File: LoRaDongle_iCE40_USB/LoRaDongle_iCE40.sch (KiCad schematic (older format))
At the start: 19 parts, among them J1 USB_A, J2 Conn_01x08

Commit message: PCB Layout V01
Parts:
- removed TP5: iCE_SCK, TestPoint:TestPoint_Pad_D2.5mm, symbol Connector:TestPoint_Small
- 5V0: renamed from TP4; footprint TestPoint:TestPoint_Pad_D2.5mm -> TestPoint:TestPoint_Pad_D1.0mm
- BUSY1: renamed from TP13; footprint TestPoint:TestPoint_Pad_D2.5mm -> TestPoint:TestPoint_Pad_D1.0mm
- C1: footprint Capacitor_SMD:C_0402_1005Metric -> Capacitor_SMD:C_0402_1005Metric_Pad0.74x0.62mm_HandSolder
- CDNE1: renamed from TP7; footprint TestPoint:TestPoint_Pad_D2.5mm -> TestPoint:TestPoint_Pad_D1.0mm
- CRST1: renamed from TP8; footprint TestPoint:TestPoint_Pad_D2.5mm -> TestPoint:TestPoint_Pad_D1.0mm
- DIO1: renamed from TP10; footprint TestPoint:TestPoint_Pad_D2.5mm -> TestPoint:TestPoint_Pad_D1.0mm
- L_SS1: renamed from TP12; value LoRa!_SS -> LoRa_!SS; footprint TestPoint:TestPoint_Pad_D2.5mm -> TestPoint:TestPoint_Pad_D1.0mm
- MISO1: renamed from TP15; footprint TestPoint:TestPoint_Pad_D2.5mm -> TestPoint:TestPoint_Pad_D1.0mm
- MOSI1: renamed from TP11; footprint TestPoint:TestPoint_Pad_D2.5mm -> TestPoint:TestPoint_Pad_D1.0mm
- R1, R2: footprint Resistor_SMD:R_0402_1005Metric -> Resistor_SMD:R_0402_1005Metric_Pad0.72x0.64mm_HandSolder
- RESET1: renamed from TP9; value LoRa_~RESET -> LoRA_~RESET; footprint TestPoint:TestPoint_Pad_D2.5mm -> TestPoint:TestPoint_Pad_D1.0mm
- SCK1: renamed from TP14; footprint TestPoint:TestPoint_Pad_D2.5mm -> TestPoint:TestPoint_Pad_D1.0mm
- SS_B1: renamed from TP6; footprint TestPoint:TestPoint_Pad_D2.5mm -> TestPoint:TestPoint_Pad_D1.0mm
- renumbered JP1 to J4
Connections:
- net ICE_CDONE: now also J2.2 (Pin_2); no longer J2.5 (Pin_5)
- net ICE_CRESET: now also J2.1 (Pin_1); no longer J2.6 (Pin_6)
- net SPI_MISO: now also J2.4 (Pin_4); no longer J2.3 (Pin_3)
- net SPI_MOSI: now also J2.5 (Pin_5); no longer J2.2 (Pin_2)
- net SPI_SCK: now also J2.6 (Pin_6); no longer J2.1 (Pin_1)
- net SPI_SS: now also J2.3 (Pin_3); no longer J2.4 (Pin_4)
- net V_USB: now also J4.1; no longer J4.3
- net V_conn: now also J4.3; no longer J4.1
- net D-: now reaches J1.2 (D-), R2.2
- net D+: now reaches J1.3 (D+), R1.2
- net USB_Interface/DM renamed USB_Interface/USB_D-
- net USB_Interface/DP renamed USB_Interface/UBS_D+
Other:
- moved on the sheet: CDNE1, CRST1, SS_B1
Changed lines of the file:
@@
 $EndComp
 $Comp
-L Device:Jumper_NC_Dual JP1
+L Device:Jumper_NC_Dual J4
 U 1 1 616C0AFF
 P 3950 1800
-F 0 "JP1" H 3950 1947 50  0000 C CNN
+F 0 "J4" H 3950 1947 50  0000 C CNN
 F 1 "Jumper" H 3950 2038 50  0000 C CNN
 F 2 "Connector_PinHeader_2.54mm:PinHeader_1x03_P2.54mm_Vertical" H 3950 1800 50  0001 C CNN
@@
 	-1   0    0    1
 $EndComp
-Text Label 4400 1800 0    50   ~ 0
-V_conn
-Text Label 3550 1800 2    50   ~ 0
+Text Label 4350 1800 0    50   ~ 0
 V_USB
 Wire Wire Line
-	3550 1800 3700 1800
-Wire Wire Line
-	4200 1800 4400 1800
+	4350 1800 4200 1800
 $Comp
 L power:+5V #PWR03
@@
 F 0 "C1" H 2150 1750 50  0000 C CNN
 F 1 "0.1uF" H 2100 2000 50  0000 C CNN
-F 2 "Capacitor_SMD:C_0402_1005Metric" H 2288 1700 50  0001 C CNN
+F 2 "Capacitor_SMD:C_0402_1005Metric_Pad0.74x0.62mm_HandSolder" H 2288 1700 50  0001 C CNN
 F 3 "~" H 2250 1850 50  0001 C CNN
 F 4 "GCM155R71C104KA55J" V 2250 1850 50  0001 C CNN "Part Number"
@@
 F 0 "R2" V 2100 3950 50  0000 C CNN
 F 1 "10R" V 2000 3950 50  0000 C CNN
-F 2 "Resistor_SMD:R_0402_1005Metric" V 1930 3950 50  0001 C CNN
+F 2 "Resistor_SMD:R_0402_1005Metric_Pad0.72x0.64mm_HandSolder" V 1930 3950 50  0001 C CNN
 F 3 "~" H 2000 3950 50  0001 C CNN
 	1    2000 3950
@@
 F 0 "R1" V 1900 3850 50  0000 C CNN
 F 1 "10R" V 2000 3850 50  0000 C CNN
-F 2 "Resistor_SMD:R_0402_1005Metric" V 1930 3850 50  0001 C CNN
+F 2 "Resistor_SMD:R_0402_1005Metric_Pad0.72x0.64mm_HandSolder" V 1930 3850 50  0001 C CNN
 F 3 "~" H 2000 3850 50  0001 C CNN
 	1    2000 3850
@@
 F0 "USB_Interface" 50
 F1 "USB_Interface.sch" 50
-F2 "DP" I L 2300 3850 50
-F3 "DM" I L 2300 3950 50
-F4 "SPI_SCK" O R 3650 3650 50
-F5 "SPI_MOSI" O R 3650 3750 50
-F6 "SPI_MISO" O R 3650 3850 50
-F7 "SPI_SS" O R 3650 3950 50
-F8 "iCE_CDONE" O R 3650 4100 50
-F9 "iCE_CRESET" O R 3650 4200 50
+F2 "SPI_SCK" O R 3650 3650 50
+F3 "SPI_MOSI" O R 3650 3750 50
+F4 "SPI_MISO" O R 3650 3850 50
+F5 "SPI_SS" O R 3650 3950 50
+F6 "iCE_CDONE" O R 3650 4100 50
+F7 "iCE_CRESET" O R 3650 4200 50
+F8 "USB_D-" I L 2300 3950 50
+F9 "UBS_D+" I L 2300 3850 50
 $EndSheet
 Text Notes 5900 1250 0    50   ~ 0
@@
 	6350 2150 6500 2150
 Wire Wire Line
-	6350 2050 6450 2050
-Wire Wire Line
-	6350 1950 6450 1950
-Wire Wire Line
-	6350 1850 6450 1850
-Wire Wire Line
-	6350 1750 6900 1750
-Wire Wire Line
-	6350 1650 6900 1650
-Wire Wire Line
 	6350 1550 6450 1550
+Wire Wire Line
+	6350 1650 6450 1650
+Wire Wire Line
+	6350 1750 6450 1750
+Wire Wire Line
+	6350 1850 6900 1850
+Wire Wire Line
+	6350 1950 6900 1950
 Text Label 6500 2250 0    50   ~ 0
 V_conn
@@
 	0    -1   -1   0
 $EndComp
+Text Label 6900 2050 0    50   ~ 0
+SPI_SCK
+Text Label 6900 1950 0    50   ~ 0
+SPI_MOSI
+Text Label 6900 1850 0    50   ~ 0
+SPI_MISO
+Text Label 6900 1750 0    50   ~ 0
+SPI_SS
+Text Label 6900 1650 0    50   ~ 0
+ICE_CDONE
 Text Label 6900 1550 0    50   ~ 0
-SPI_SCK
-Text Label 6900 1650 0    50   ~ 0
-SPI_MOSI
-Text Label 6900 1750 0    50   ~ 0
-SPI_MISO
-Text Label 6900 1850 0    50   ~ 0
-SPI_SS
-Text Label 6900 1950 0    50   ~ 0
-ICE_CDONE
-Text Label 6900 2050 0    50   ~ 0
 ICE_CRESET
 Wire Wire Line
@@
 $EndSheet
 $Comp
-L Connector:TestPoint_Small TP12
+L Connector:TestPoint_Small L_SS1
 U 1 1 61D568D0
 P 6950 4250
-F 0 "TP12" H 6998 4296 50  0000 L CNN
-F 1 "LoRa!_SS" H 6998 4205 50  0000 L CNN
-F 2 "TestPoint:TestPoint_Pad_D2.5mm" H 7150 4250 50  0001 C CNN
+F 0 "L_SS1" H 6998 4296 50  0000 L CNN
+F 1 "LoRa_!SS" H 6998 4205 50  0000 L CNN
+F 2 "TestPoint:TestPoint_Pad_D1.0mm" H 7150 4250 50  0001 C CNN
 F 3 "~" H 7150 4250 50  0001 C CNN
 	1    6950 4250
@@
 	6950 4250 8750 4250
 $Comp
-L Connector:TestPoint_Small TP15
+L Connector:TestPoint_Small MISO1
 U 1 1 61D57118
 P 8050 4150
-F 0 "TP15" H 8098 4196 50  0000 L CNN
+F 0 "MISO1" H 8098 4196 50  0000 L CNN
 F 1 "LoRA_MISO" H 8098 4105 50  0000 L CNN
-F 2 "TestPoint:TestPoint_Pad_D2.5mm" H 8250 4150 50  0001 C CNN
+F 2 "TestPoint:TestPoint_Pad_D1.0mm" H 8250 4150 50  0001 C CNN
 F 3 "~" H 8250 4150 50  0001 C CNN
 	1    8050 4150
@@
 	8050 4150 8750 4150
 $Comp
-L Connector:TestPoint_Small TP11
+L Connector:TestPoint_Small MOSI1
 U 1 1 61D572CB
 P 6950 4050
-F 0 "TP11" H 6998 4096 50  0000 L CNN
+F 0 "MOSI1" H 6998 4096 50  0000 L CNN
 F 1 "LoRa_MOSI" H 6998 4005 50  0000 L CNN
-F 2 "TestPoint:TestPoint_Pad_D2.5mm" H 7150 4050 50  0001 C CNN
+F 2 "TestPoint:TestPoint_Pad_D1.0mm" H 7150 4050 50  0001 C CNN
 F 3 "~" H 7150 4050 50  0001 C CNN
 	1    6950 4050
@@
 	6950 4050 8750 4050
 $Comp
-L Connector:TestPoint_Small TP14
+L Connector:TestPoint_Small SCK1
 U 1 1 61D57576
 P 8050 3950
-F 0 "TP14" H 8098 3996 50  0000 L CNN
+F 0 "SCK1" H 8098 3996 50  0000 L CNN
 F 1 "LoRa_SCK" H 8098 3905 50  0000 L CNN
-F 2 "TestPoint:TestPoint_Pad_D2.5mm" H 8250 3950 50  0001 C CNN
+F 2 "TestPoint:TestPoint_Pad_D1.0mm" H 8250 3950 50  0001 C CNN
 F 3 "~" H 8250 3950 50  0001 C CNN
 	1    8050 3950
@@
 	8050 3950 8750 3950
 $Comp
-L Connector:TestPoint_Small TP10
+L Connector:TestPoint_Small DIO1
 U 1 1 61D57700
 P 6950 3800
-F 0 "TP10" H 6998 3846 50  0000 L CNN
+F 0 "DIO1" H 6998 3846 50  0000 L CNN
 F 1 "Radio_DIO1" H 6998 3755 50  0000 L CNN
-F 2 "TestPoint:TestPoint_Pad_D2.5mm" H 7150 3800 50  0001 C CNN
+F 2 "TestPoint:TestPoint_Pad_D1.0mm" H 7150 3800 50  0001 C CNN
 F 3 "~" H 7150 3800 50  0001 C CNN
 	1    6950 3800
@@
 	6950 3800 8750 3800
 $Comp
-L Connector:TestPoint_Small TP13
+L Connector:TestPoint_Small BUSY1
 U 1 1 61D57954
 P 8050 3700
-F 0 "TP13" H 8098 3746 50  0000 L CNN
+F 0 "BUSY1" H 8098 3746 50  0000 L CNN
 F 1 "Radio_Busy" H 8098 3655 50  0000 L CNN
-F 2 "TestPoint:TestPoint_Pad_D2.5mm" H 8250 3700 50  0001 C CNN
+F 2 "TestPoint:TestPoint_Pad_D1.0mm" H 8250 3700 50  0001 C CNN
 F 3 "~" H 8250 3700 50  0001 C CNN
 	1    8050 3700
@@
 	8050 3700 8750 3700
 $Comp
-L Connector:TestPoint_Small TP9
+L Connector:TestPoint_Small RESET1
 U 1 1 61D57B0F
 P 6950 3600
-F 0 "TP9" H 6998 3652 50  0000 L CNN
-F 1 "LoRa_~RESET" H 6998 3554 50  0000 L CNN
-F 2 "TestPoint:TestPoint_Pad_D2.5mm" H 7150 3600 50  0001 C CNN
+F 0 "RESET1" H 6998 3652 50  0000 L CNN
+F 1 "LoRA_~RESET" H 6998 3554 50  0000 L CNN
+F 2 "TestPoint:TestPoint_Pad_D1.0mm" H 7150 3600 50  0001 C CNN
 F 3 "~" H 7150 3600 50  0001 C CNN
 	1    6950 3600
@@
 Text Label 4250 3650 0    50   ~ 0
 SPI_SCK
-$Comp
-L Connector:TestPoint TP4
+Connection ~ 3950 1550
+Wire Wire Line
+	3950 1550 3950 1500
+$Comp
+L Connector:TestPoint_Small SS_B1
+U 1 1 61DA4E99
+P 6450 1750
+F 0 "SS_B1" H 6500 1800 50  0000 L CNN
+F 1 "iCE_SS_B" H 6498 1705 50  0001 L CNN
+F 2 "TestPoint:TestPoint_Pad_D1.0mm" H 6650 1750 50  0001 C CNN
+F 3 "~" H 6650 1750 50  0001 C CNN
+	1    6450 1750
+	1    0    0    -1
+$EndComp
+Connection ~ 6450 1750
+Wire Wire Line
+	6450 1750 6900 1750
+$Comp
+L Connector:TestPoint_Small CDNE1
+U 1 1 61DB206F
+P 6450 1650
+F 0 "CDNE1" H 6500 1700 50  0000 L CNN
+F 1 "iCE_CDONE" H 6498 1605 50  0001 L CNN
+F 2 "TestPoint:TestPoint_Pad_D1.0mm" H 6650 1650 50  0001 C CNN
+F 3 "~" H 6650 1650 50  0001 C CNN
+	1    6450 1650
+	1    0    0    -1
+$EndComp
+Connection ~ 6450 1650
+Wire Wire Line
+	6450 1650 6900 1650
+$Comp
+L Connector:TestPoint_Small CRST1
+U 1 1 61DB235D
+P 6450 1550
+F 0 "CRST1" H 6500 1600 50  0000 L CNN
+F 1 "iCE_CRESET" H 6498 1505 50  0001 L CNN
+F 2 "TestPoint:TestPoint_Pad_D1.0mm" H 6650 1550 50  0001 C CNN
+F 3 "~" H 6650 1550 50  0001 C CNN
+	1    6450 1550
+	1    0    0    -1
+$EndComp
+Connection ~ 6450 1550
+Wire Wire Line
+	6450 1550 6900 1550
+Text Label 1650 3850 0    50   ~ 0
+D+
+Text Label 1650 3950 0    50   ~ 0
+D-
+Wire Wire Line
+	6350 2050 6900 2050
+Wire Wire Line
+	3700 1800 3500 1800
+Text Label 3500 1800 2    50   ~ 0
+V_conn
+$Comp
+L Connector:TestPoint 5V0
 U 1 1 61DA3031
 P 3950 1550
-F 0 "TP4" V 3904 1738 50  0000 L CNN
+F 0 "5V0" V 3904 1738 50  0000 L CNN
 F 1 "5V" V 3995 1738 50  0000 L CNN
-F 2 "TestPoint:TestPoint_Pad_D2.5mm" H 4150 1550 50  0001 C CNN
+F 2 "TestPoint:TestPoint_Pad_D1.0mm" H 4150 1550 50  0001 C CNN
 F 3 "~" H 4150 1550 50  0001 C CNN
 	1    3950 1550
 	0    1    1    0
 $EndComp
-Connection ~ 3950 1550
-Wire Wire Line
-	3950 1550 3950 1500
-$Comp
-L Connector:TestPoint_Small TP5
-U 1 1 61DA426C
-P 6450 1550
-F 0 "TP5" H 6500 1600 50  0000 L CNN
-F 1 "iCE_SCK" H 6498 1505 50  0001 L CNN
-F 2 "TestPoint:TestPoint_Pad_D2.5mm" H 6650 1550 50  0001 C CNN
-F 3 "~" H 6650 1550 50  0001 C CNN
-	1    6450 1550
-	1    0    0    -1
-$EndComp
-Connection ~ 6450 1550
-Wire Wire Line
-	6450 1550 6900 1550
-$Comp
-L Connector:TestPoint_Small TP6
-U 1 1 61DA4E99
-P 6450 1850
-F 0 "TP6" H 6500 1900 50  0000 L CNN
-F 1 "iCE_SS_B" H 6498 1805 50  0001 L CNN
-F 2 "TestPoint:TestPoint_Pad_D2.5mm" H 6650 1850 50  0001 C CNN
-F 3 "~" H 6650 1850 50  0001 C CNN
-	1    6450 1850
-	1    0    0    -1
-$EndComp
-Connection ~ 6450 1850
-Wire Wire Line
-	6450 1850 6900 1850
-$Comp
-L Connector:TestPoint_Small TP7
-U 1 1 61DB206F
-P 6450 1950
-F 0 "TP7" H 6500 2000 50  0000 L CNN
-F 1 "iCE_CDONE" H 6498 1905 50  0001 L CNN
-F 2 "TestPoint:TestPoint_Pad_D2.5mm" H 6650 1950 50  0001 C CNN
-F 3 "~" H 6650 1950 50  0001 C CNN
-	1    6450 1950
-	1    0    0    -1
-$EndComp
-Connection ~ 6450 1950
-Wire Wire Line
-	6450 1950 6900 1950
-$Comp
-L Connector:TestPoint_Small TP8
-U 1 1 61DB235D
-P 6450 2050
-F 0 "TP8" H 6500 2100 50  0000 L CNN
-F 1 "iCE_CRESET" H 6498 2005 50  0001 L CNN
-F 2 "TestPoint:TestPoint_Pad_D2.5mm" H 6650 2050 50  0001 C CNN
-F 3 "~" H 6650 2050 50  0001 C CNN
-	1    6450 2050
-	1    0    0    -1
-$EndComp
-Connection ~ 6450 2050
-Wire Wire Line
-	6450 2050 6900 2050
 $EndSCHEMATC

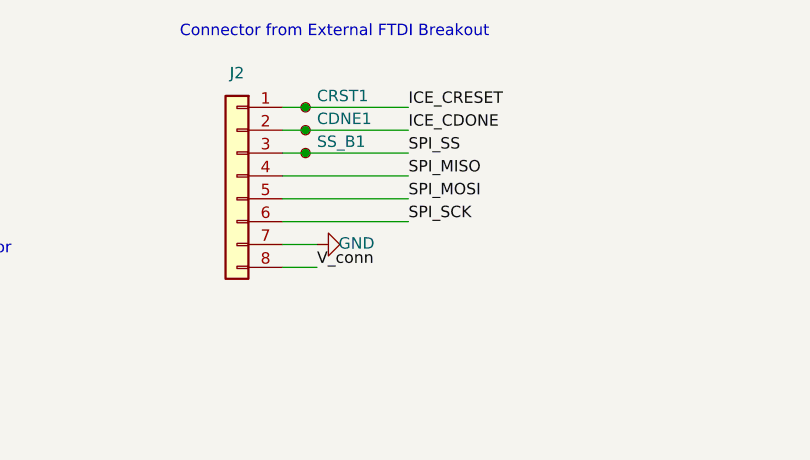
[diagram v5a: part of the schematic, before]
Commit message: breakout of bga part
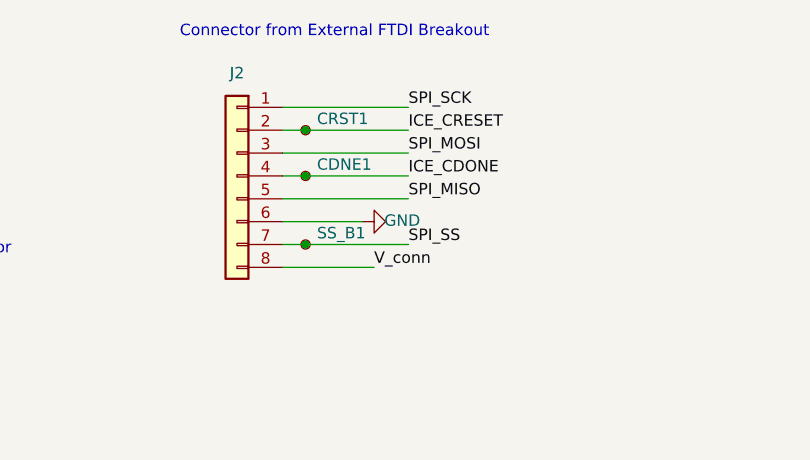
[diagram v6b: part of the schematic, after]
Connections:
- net GND: now also J2.6 (Pin_6); no longer J2.7 (Pin_7)
- net ICE_CDONE: now also J2.4 (Pin_4); no longer J2.2 (Pin_2)
- net ICE_CRESET: now also J2.2 (Pin_2); no longer J2.1 (Pin_1)
- net SPI_MISO: now also J2.5 (Pin_5); no longer J2.4 (Pin_4)
- net SPI_MOSI: now also J2.3 (Pin_3); no longer J2.5 (Pin_5)
- net SPI_SCK: now also J2.1 (Pin_1); no longer J2.6 (Pin_6)
- net SPI_SS: now also J2.7 (Pin_7); no longer J2.3 (Pin_3)
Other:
- moved on the sheet: CDNE1, CRST1, SS_B1
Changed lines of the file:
@@
 	6750 4550 8750 4550
 Wire Wire Line
-	6350 2250 6500 2250
-Wire Wire Line
-	6350 2150 6500 2150
-Wire Wire Line
-	6350 1550 6450 1550
+	6350 2250 6750 2250
+Wire Wire Line
+	6350 2050 6700 2050
 Wire Wire Line
 	6350 1650 6450 1650
 Wire Wire Line
-	6350 1750 6450 1750
-Wire Wire Line
-	6350 1850 6900 1850
+	6350 1850 6450 1850
+Wire Wire Line
+	6350 2150 6450 2150
 Wire Wire Line
 	6350 1950 6900 1950
-Text Label 6500 2250 0    50   ~ 0
+Wire Wire Line
+	6350 1750 6900 1750
+Text Label 6750 2250 0    50   ~ 0
 V_conn
 $Comp
 L power:GND #PWR02
 U 1 1 61B86EAD
-P 6500 2150
-F 0 "#PWR02" H 6500 1900 50  0001 C CNN
-F 1 "GND" V 6505 1977 50  0000 C CNN
-F 2 "" H 6500 2150 50  0001 C CNN
-F 3 "" H 6500 2150 50  0001 C CNN
-	1    6500 2150
+P 6700 2050
+F 0 "#PWR02" H 6700 1800 50  0001 C CNN
+F 1 "GND" V 6705 1877 50  0000 C CNN
+F 2 "" H 6700 2050 50  0001 C CNN
+F 3 "" H 6700 2050 50  0001 C CNN
+	1    6700 2050
 	0    -1   -1   0
 $EndComp
-Text Label 6900 2050 0    50   ~ 0
+Text Label 6900 1550 0    50   ~ 0
 SPI_SCK
+Text Label 6900 1750 0    50   ~ 0
+SPI_MOSI
 Text Label 6900 1950 0    50   ~ 0
-SPI_MOSI
+SPI_MISO
+Text Label 6900 2150 0    50   ~ 0
+SPI_SS
 Text Label 6900 1850 0    50   ~ 0
-SPI_MISO
-Text Label 6900 1750 0    50   ~ 0
-SPI_SS
-Text Label 6900 1650 0    50   ~ 0
 ICE_CDONE
-Text Label 6900 1550 0    50   ~ 0
-ICE_CRESET
 Wire Wire Line
 	3650 3650 4850 3650
@@
 L Connector:TestPoint_Small SS_B1
 U 1 1 61DA4E99
-P 6450 1750
-F 0 "SS_B1" H 6500 1800 50  0000 L CNN
-F 1 "iCE_SS_B" H 6498 1705 50  0001 L CNN
-F 2 "TestPoint:TestPoint_Pad_D1.0mm" H 6650 1750 50  0001 C CNN
-F 3 "~" H 6650 1750 50  0001 C CNN
-	1    6450 1750
-	1    0    0    -1
-$EndComp
-Connection ~ 6450 1750
-Wire Wire Line
-	6450 1750 6900 1750
+P 6450 2150
+F 0 "SS_B1" H 6500 2200 50  0000 L CNN
+F 1 "iCE_SS_B" H 6498 2105 50  0001 L CNN
+F 2 "TestPoint:TestPoint_Pad_D1.0mm" H 6650 2150 50  0001 C CNN
+F 3 "~" H 6650 2150 50  0001 C CNN
+	1    6450 2150
+	1    0    0    -1
+$EndComp
+Connection ~ 6450 2150
+Wire Wire Line
+	6450 2150 6900 2150
 $Comp
 L Connector:TestPoint_Small CDNE1
 U 1 1 61DB206F
+P 6450 1850
+F 0 "CDNE1" H 6500 1900 50  0000 L CNN
+F 1 "iCE_CDONE" H 6498 1805 50  0001 L CNN
+F 2 "TestPoint:TestPoint_Pad_D1.0mm" H 6650 1850 50  0001 C CNN
+F 3 "~" H 6650 1850 50  0001 C CNN
+	1    6450 1850
+	1    0    0    -1
+$EndComp
+Connection ~ 6450 1850
+Wire Wire Line
+	6450 1850 6900 1850
+$Comp
+L Connector:TestPoint_Small CRST1
+U 1 1 61DB235D
 P 6450 1650
-F 0 "CDNE1" H 6500 1700 50  0000 L CNN
-F 1 "iCE_CDONE" H 6498 1605 50  0001 L CNN
+F 0 "CRST1" H 6500 1700 50  0000 L CNN
+F 1 "iCE_CRESET" H 6498 1605 50  0001 L CNN
 F 2 "TestPoint:TestPoint_Pad_D1.0mm" H 6650 1650 50  0001 C CNN
 F 3 "~" H 6650 1650 50  0001 C CNN
@@
 	1    0    0    -1
 $EndComp
-Connection ~ 6450 1650
-Wire Wire Line
-	6450 1650 6900 1650
-$Comp
-L Connector:TestPoint_Small CRST1
-U 1 1 61DB235D
-P 6450 1550
-F 0 "CRST1" H 6500 1600 50  0000 L CNN
-F 1 "iCE_CRESET" H 6498 1505 50  0001 L CNN
-F 2 "TestPoint:TestPoint_Pad_D1.0mm" H 6650 1550 50  0001 C CNN
-F 3 "~" H 6650 1550 50  0001 C CNN
-	1    6450 1550
-	1    0    0    -1
-$EndComp
-Connection ~ 6450 1550
-Wire Wire Line
-	6450 1550 6900 1550
 Text Label 1650 3850 0    50   ~ 0
 D+
@@
 D-
 Wire Wire Line
-	6350 2050 6900 2050
+	6350 1550 6900 1550
 Wire Wire Line
 	3700 1800 3500 1800
@@
 	0    1    1    0
 $EndComp
+Connection ~ 6450 1650
+Wire Wire Line
+	6450 1650 6900 1650
+Text Label 6900 1650 0    50   ~ 0
+ICE_CRESET
 $EndSCHEMATC
